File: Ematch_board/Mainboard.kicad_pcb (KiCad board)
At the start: 2 copper layers, 57.3 x 53.3 mm, 137 parts, among them J1 Conn_01x02_Male, J10 Conn_01x02_Male, J2 Conn_01x02_Male, J3 Conn_01x02_Male, J4 Conn_01x02_Male, J5 Conn_01x02_Male, J6 Conn_01x02_Male, J7 Conn_01x05_Male, J8 USB_C_Receptacle_USB2.0, J9 Conn_01x02_Male, Q1 MMDT2222A, Q2 MMDT2222A, Q51 PMV20ENR, Q52 PMV20ENR, Q53 PMV20ENR, Q54 PMV20ENR, Q55 PMV20ENR, Q56 PMV20ENR, U1 LTV-247, U2 LTC4411, U3 RT9025-25GSP, U4 LTC4411, U5 SN65HVD230, U6 CP2102-GMR-QFN28

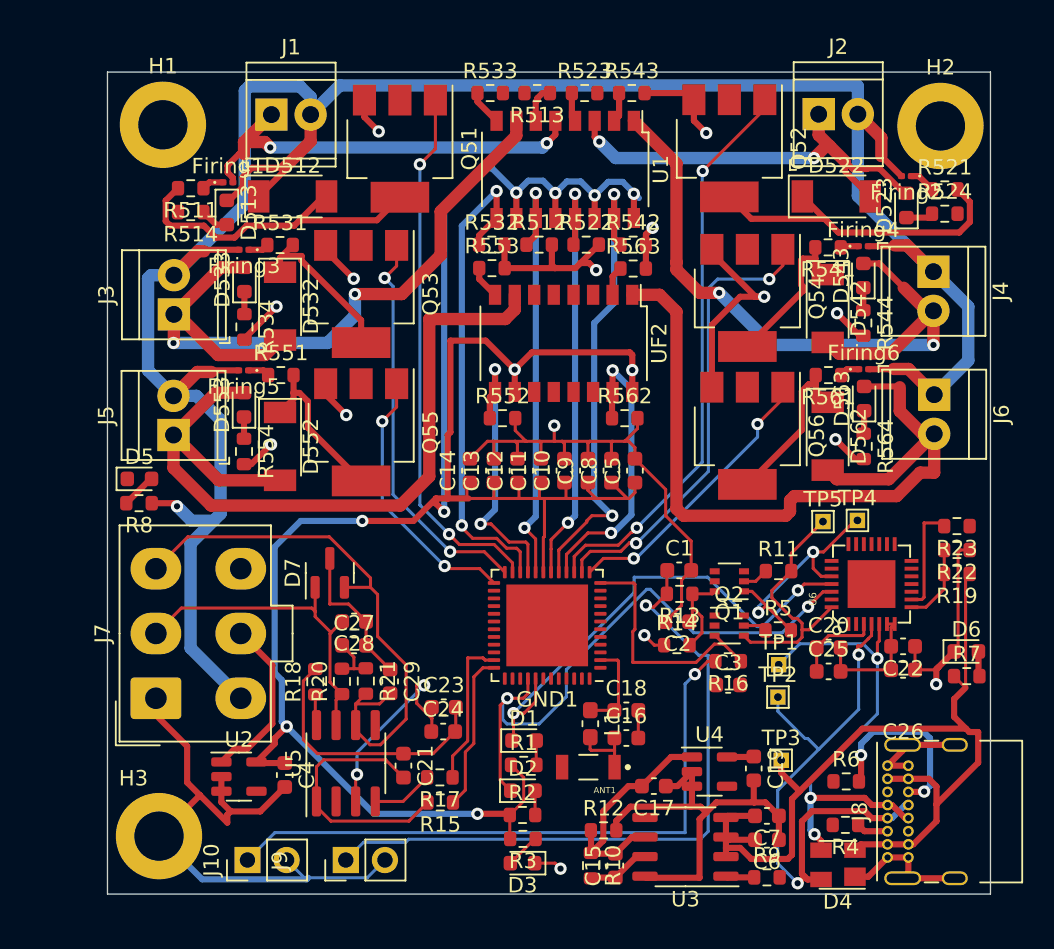
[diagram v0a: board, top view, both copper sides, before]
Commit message: removed ground traces
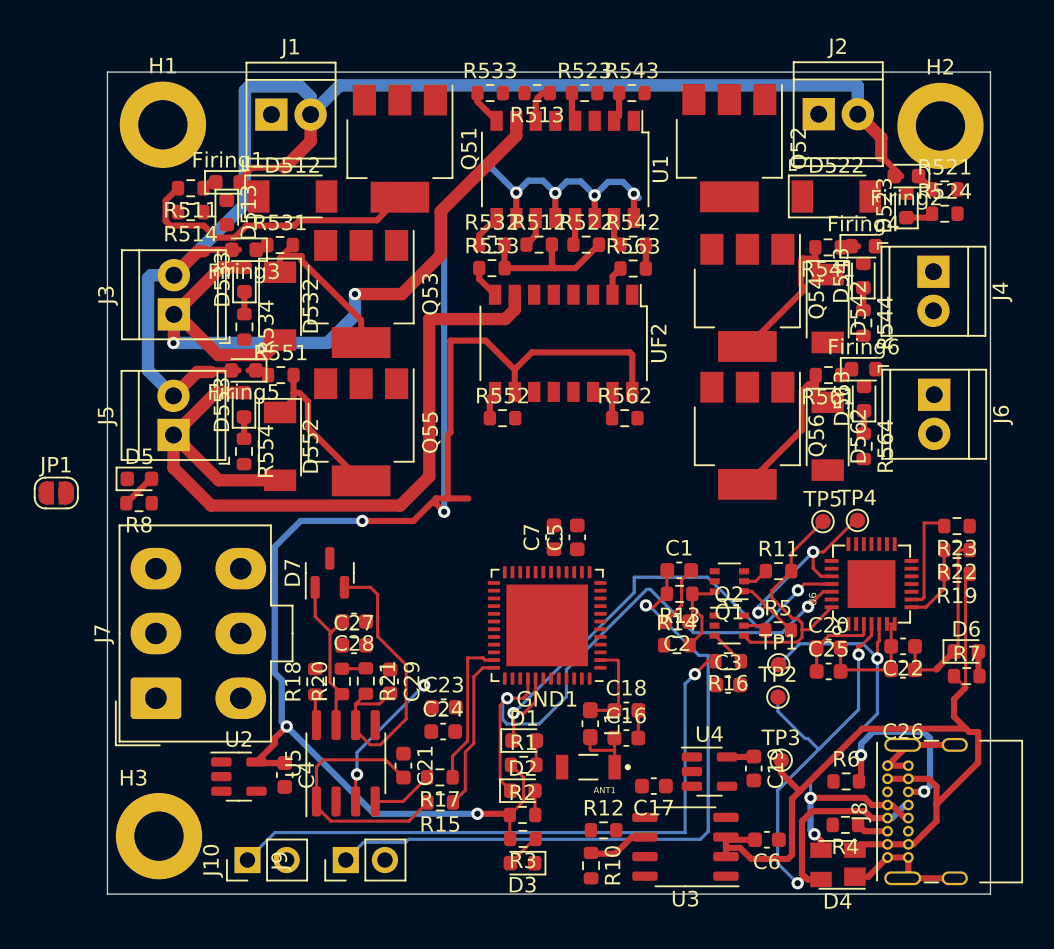
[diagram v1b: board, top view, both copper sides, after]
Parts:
- removed C10: 10uF, Capacitor_SMD:C_0603_1608Metric
- removed C11, C8: 1uF, Capacitor_SMD:C_0603_1608Metric
- removed C12, C13, C14, C15: 0.1uF, Capacitor_SMD:C_0603_1608Metric
- removed C9: 100pF, Capacitor_SMD:C_0603_1608Metric
- removed R9: 100k, Resistor_SMD:R_0603_1608Metric
- added JP1: SolderJumper_2_Open, Jumper:SolderJumper-2_P1.3mm_Open_RoundedPad1.0x1.5mm, F.Cu at (114.7, 96.8)
- C16: value 1.5pF -> 33pF
- C18: value 1.2pF -> 100pF
- C2: value 1nF -> 0.1uF
- C5: value 0.1uF -> 10uF
- C7: value 1uF -> 0.1uF
- Firing1, Firing2, Firing3, Firing4, Firing5, Firing6: footprint Diode_SMD:D_0201_0603Metric -> LED_SMD:LED_0603_1608Metric
- J7: value Conn_01x05_Male -> Conn_01x06_Female
- R10: value 147k -> 56k
- R12: value 47k -> 10K
- R15, R17: value 90 -> 120
- TP1, TP2, TP3, TP4, TP5: footprint TestPoint:TestPoint_THTPad_1.0x1.0mm_Drill0.5mm -> TestPoint:TestPoint_Pad_D1.0mm
- moved C7 22.7 mm to (146.9, 99.7), turned to 90 degrees
- moved C5 5.72 mm to (148.4, 99.7)
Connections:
- net Net-(C27-Pad1) renamed /Vref
- ANT1 pad 2: GND -> (no net)
- C7 pad 1: GND -> +3V3
- C7 pad 2: VBUS -> GND
- GND1 pad 12: /BOOT -> /Nuke 1
- GND1 pad 23: /Nuke 1 -> /BOOT
- GND1 pad 9: unconnected-(GND1-Pad9) -> /EN
- J7 pad 2: /CAN_HIGH -> GND
- J7 pad 3: /CAN_LOW -> Net-(J7-Pad3)
- J7 pad 5: Net-(U2-Pad1) -> /CAN_HIGH
- J7 pad 6: (no net) -> /CAN_LOW
- R8 pad 1: /24V -> +24V
- U2 pad 1: Net-(U2-Pad1) -> Net-(J7-Pad3)
- U3 pad 1: Net-(R9-Pad1) -> unconnected-(U3-Pad1)
- U3 pad 4: VBUS -> unconnected-(U3-Pad4)
- U5 pad 5: unconnected-(U5-Pad5) -> Net-(U5-Pad5)
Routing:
- net GND: track 219.0 -> 50.3 mm, vias 14 -> 0
- net /24V: track 154.9 -> 90.6 mm, vias 1 -> 0
- net Net-(D562-Pad2): track 52.2 -> 0.00 mm
- net Net-(D542-Pad2): track 45.8 -> 0.00 mm, vias 2 -> 0
- net /Nuke 2: track 37.0 -> 0.00 mm, vias 2 -> 0
- net /Nuke 1: track 34.8 -> 0.00 mm, vias 2 -> 0
- net +3V3: track 164.1 -> 133.0 mm, vias 13 -> 10
- net /ematch/Cont3: track 32.5 -> 2.20 mm, vias 2 -> 0
- net /Nuke 4: track 29.8 -> 0.00 mm, vias 2 -> 0
- net Net-(D512-Pad2): track 29.4 -> 0.00 mm, vias 2 -> 0
- net /ematch/Cont4: track 31.2 -> 1.90 mm, vias 2 -> 0
- net Net-(D522-Pad2): track 28.8 -> 0.00 mm, vias 2 -> 0
- net /ematch/Cont2: track 28.5 -> 1.62 mm, vias 2 -> 0
- net /ematch/Cont1: track 28.8 -> 1.98 mm, vias 2 -> 0
- net /Nuke 3: track 26.0 -> 0.00 mm, vias 2 -> 0
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
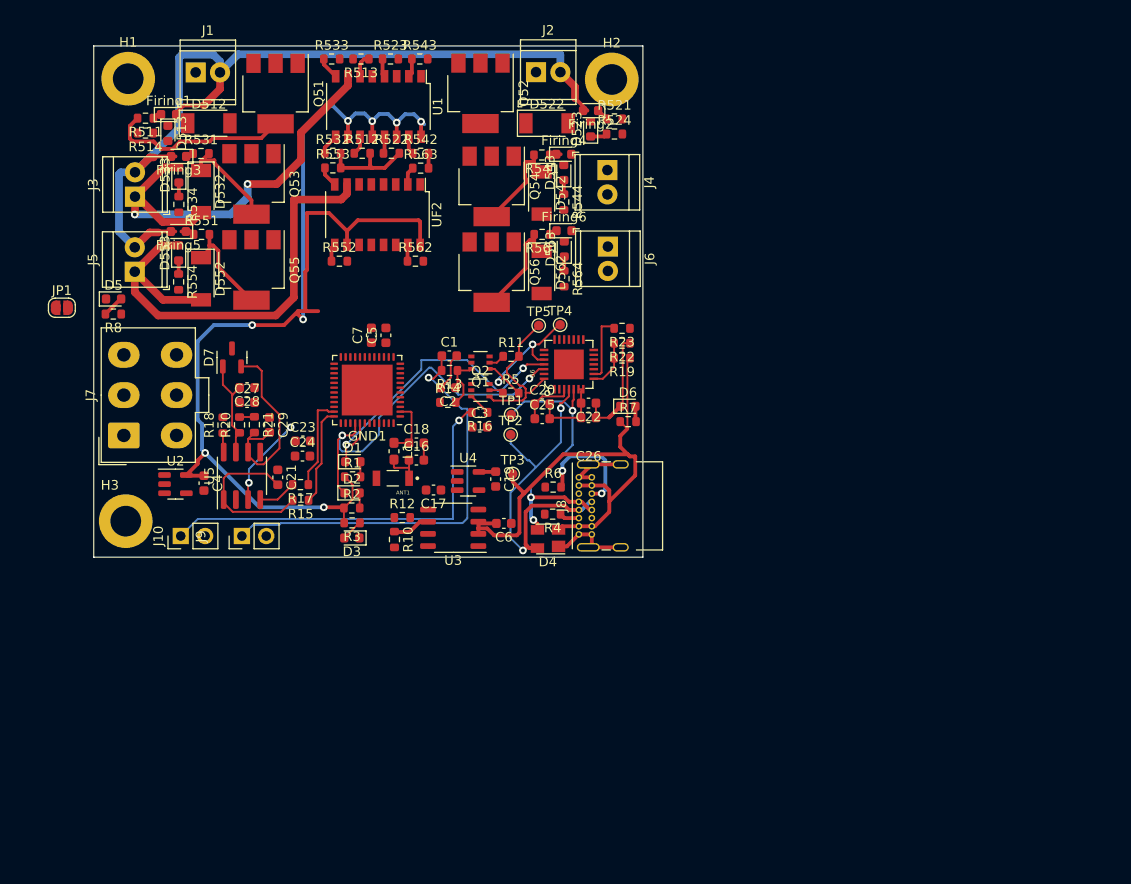
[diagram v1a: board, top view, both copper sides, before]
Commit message: routed thicker 24V traces and moved some components
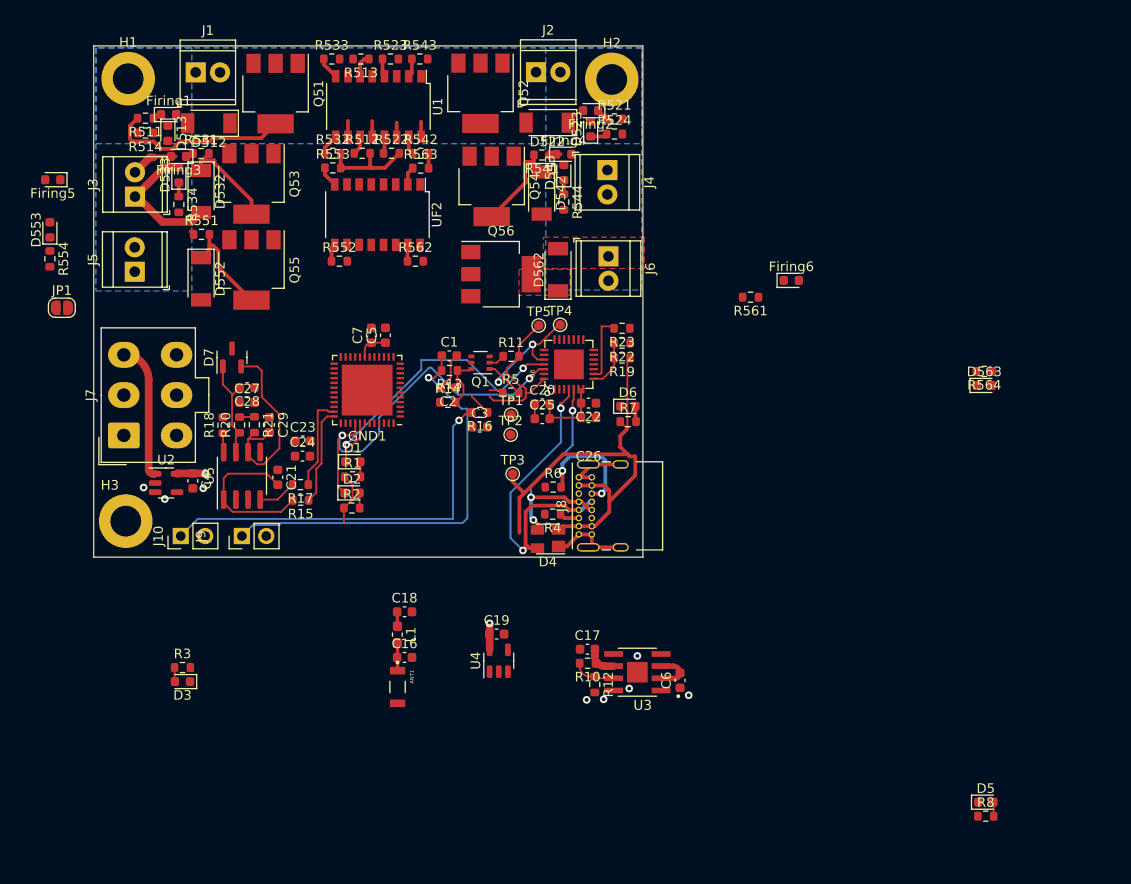
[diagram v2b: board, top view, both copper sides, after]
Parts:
- removed Q2: MMDT2222A, Package_TO_SOT_SMD:SOT-363_SC-70-6
- U3: footprint Package_SO:SOP-8_3.9x4.9mm_P1.27mm -> iclr:SOIC127P599X175-9N
- moved D5 105.0 mm to (211.0, 148.3)
- moved R8 104.9 mm to (211.0, 149.8), turned to 0 degrees
- moved D563 46.0 mm to (210.8, 104.9), turned to 0 degrees
- moved R564 44.9 mm to (210.8, 103.4), turned to 180 degrees
- moved R12 26.6 mm to (170.2, 136.1), turned to -90 degrees
- moved C6 24.6 mm to (179.1, 135.7), turned to 90 degrees
- moved U3 24.4 mm to (174.7, 134.8)
- moved Firing6 24.3 mm to (190.7, 94.0)
- moved R10 23.9 mm to (169.5, 133.9), turned to 180 degrees
- moved R3 23.2 mm to (127.2, 134.3), turned to 0 degrees
- moved D3 23.2 mm to (127.2, 135.8)
- moved C17 23.1 mm to (169.4, 132.4), turned to 0 degrees
- moved R561 22.7 mm to (186.4, 95.7)
- moved ANT1 21.8 mm to (149.7, 136.3), turned to -90 degrees
- moved C16 20.6 mm to (150.4, 133.3)
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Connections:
- C19 pad 1: /3.3V -> +3V3
- C20 pad 2: /3.3V -> +3V3
- C22 pad 2: /3.3V -> +3V3
- C25 pad 2: /3.3V -> +3V3
- C26 pad 2: /3.3V -> +3V3
- Q1 pad 3: (no net) -> /BOOT
- Q1 pad 4: (no net) -> /DTR
- Q52 pad 2: Net-(D522-Pad1) -> Net-(Q52-Pad2)
- Q52 pad 4: Net-(D522-Pad1) -> Net-(Q52-Pad2)
- R521 pad 2: Net-(D522-Pad1) -> Net-(Q52-Pad2)
- U4 pad 5: /3.3V -> +3V3
- U6 pad 6: /3.3V -> +3V3
- U6 pad 7: /3.3V -> +3V3
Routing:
- net +3V3: track 133.0 -> 29.2 mm, vias 10 -> 2
- net /24V: track 90.6 -> 5.56 mm
- net Net-(D552-Pad2): track 51.3 -> 0.00 mm
- net Net-(D532-Pad2): track 47.1 -> 14.0 mm, vias 2 -> 0
- net GND: track 50.3 -> 32.3 mm, vias 0 -> 8
- net Net-(J7-Pad3): track 0.00 -> 14.2 mm
- net Net-(D562-Pad1): track 10.7 -> 0.00 mm
- net /3.3V: track 10.00 -> 0.00 mm
- net /Data-: track 31.1 -> 23.7 mm
- net /Data+: track 37.8 -> 33.2 mm
- net Net-(R10-Pad2): track 0.00 -> 4.53 mm
- net /LNA_IN: track 5.68 -> 1.52 mm
- net VBUS: track 57.1 -> 53.8 mm
- net Net-(D563-Pad1): track 1.46 -> 0.00 mm
- net Net-(D553-Pad1): track 1.41 -> 0.00 mm
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- added copper zone on In2.Cu, net +3V3
- added copper zone on B.Cu, net /24V
- added copper zone on In1.Cu, net GND
- added copper zone on F.Cu, net Net-(D562-Pad1)
- added copper zone on F.Cu, net Net-(D562-Pad2)
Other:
- copper layers 2 -> 4

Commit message: changed schottky diode FP and rearranged mosfets + screw terminals
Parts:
- D512, D522, D532, D542, D552, D562: footprint Diode_SMD:D_SOD-128 -> Package_TO_SOT_SMD:TO-277B
- moved Firing4 51.4 mm to (216.9, 93.2)
- moved R541 50.8 mm to (213.9, 93.2)
- moved J6 46.3 mm to (216.6, 102.6)
- moved D562 45.9 mm to (210.6, 105.3), turned to 0 degrees
- moved D542 45.9 mm to (210.2, 90.7), turned to 0 degrees
- moved Q56 45.2 mm to (203.9, 105.7)
- moved J4 45.0 mm to (216.2, 88.0)
- moved Q54 44.6 mm to (203.6, 91.0), turned to 0 degrees
- moved D543 39.7 mm to (206.5, 86.7), turned to 0 degrees
- moved R544 36.6 mm to (203.5, 86.7), turned to 180 degrees
- moved R561 30.4 mm to (214.3, 107.9)
- moved Firing6 30.0 mm to (217.3, 107.9)
- moved C19 14.0 mm to (162.9, 144.5)
- moved U4 14.0 mm to (163.1, 147.3)
- moved C17 12.4 mm to (170.3, 144.8)
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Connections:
- D512 pad 2: Net-(D512-Pad2) -> Net-(D512-Pad1)
- D513 pad 2: Net-(D512-Pad2) -> Net-(D512-Pad1)
- D522 pad 1: Net-(Q52-Pad2) -> Net-(D523-Pad2)
- D522 pad 2: Net-(D522-Pad2) -> Net-(D523-Pad2)
- D523 pad 2: Net-(D522-Pad2) -> Net-(D523-Pad2)
- D532 pad 1: Net-(D532-Pad1) -> Net-(D533-Pad2)
- D532 pad 2: Net-(D532-Pad2) -> Net-(D533-Pad2)
- D533 pad 2: Net-(D532-Pad2) -> Net-(D533-Pad2)
- D542 pad 1: Net-(D542-Pad1) -> Net-(D543-Pad2)
- D542 pad 2: Net-(D542-Pad2) -> Net-(D543-Pad2)
- D543 pad 2: Net-(D542-Pad2) -> Net-(D543-Pad2)
- D552 pad 2: Net-(D552-Pad2) -> Net-(D552-Pad1)
- D553 pad 2: Net-(D552-Pad2) -> Net-(D552-Pad1)
- D562 pad 1: Net-(D562-Pad1) -> Net-(D563-Pad2)
- D562 pad 2: Net-(D562-Pad2) -> Net-(D563-Pad2)
- D563 pad 2: Net-(D562-Pad2) -> Net-(D563-Pad2)
- J1 pad 1: Net-(D512-Pad2) -> Net-(D512-Pad1)
- J2 pad 1: Net-(D522-Pad2) -> Net-(D523-Pad2)
- J3 pad 1: Net-(D532-Pad2) -> Net-(D533-Pad2)
- J4 pad 1: Net-(D542-Pad2) -> Net-(D543-Pad2)
- J5 pad 1: Net-(D552-Pad2) -> Net-(D552-Pad1)
- J6 pad 1: Net-(D562-Pad2) -> Net-(D563-Pad2)
- Q1 pad 5: (no net) -> Net-(Q1-Pad5)
- Q51 pad 2: Net-(D512-Pad1) -> Net-(D512-Pad3)
- Q51 pad 4: Net-(D512-Pad1) -> Net-(D512-Pad3)
- Q52 pad 2: Net-(Q52-Pad2) -> Net-(D522-Pad3)
- Q52 pad 4: Net-(Q52-Pad2) -> Net-(D522-Pad3)
- Q53 pad 2: Net-(D532-Pad1) -> Net-(D532-Pad3)
- Q53 pad 4: Net-(D532-Pad1) -> Net-(D532-Pad3)
- Q54 pad 2: Net-(D542-Pad1) -> Net-(D542-Pad3)
- Q54 pad 4: Net-(D542-Pad1) -> Net-(D542-Pad3)
- Q55 pad 2: Net-(D552-Pad1) -> Net-(D552-Pad3)
- Q55 pad 4: Net-(D552-Pad1) -> Net-(D552-Pad3)
- Q56 pad 2: Net-(D562-Pad1) -> Net-(D562-Pad3)
- Q56 pad 4: Net-(D562-Pad1) -> Net-(D562-Pad3)
- R511 pad 2: Net-(D512-Pad1) -> Net-(D512-Pad3)
- R521 pad 2: Net-(Q52-Pad2) -> Net-(D522-Pad3)
- R531 pad 2: Net-(D532-Pad1) -> Net-(D532-Pad3)
- R541 pad 2: Net-(D542-Pad1) -> Net-(D542-Pad3)
- R551 pad 2: Net-(D552-Pad1) -> Net-(D552-Pad3)
- R561 pad 2: Net-(D562-Pad1) -> Net-(D562-Pad3)
- U1 pad 1: Net-(D542-Pad2) -> Net-(D543-Pad2)
- U1 pad 3: Net-(D522-Pad2) -> Net-(D523-Pad2)
- U1 pad 5: Net-(D512-Pad2) -> Net-(D512-Pad1)
- U1 pad 7: Net-(D532-Pad2) -> Net-(D533-Pad2)
- UF2 pad 1: Net-(D562-Pad2) -> Net-(D563-Pad2)
- UF2 pad 7: Net-(D552-Pad2) -> Net-(D552-Pad1)
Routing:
- net Net-(D512-Pad3): track 0.00 -> 19.2 mm
- net Net-(D512-Pad1): track 19.2 -> 0.00 mm
- net Net-(D533-Pad2): track 0.00 -> 14.0 mm
- net Net-(D532-Pad2): track 14.0 -> 0.00 mm
- net Net-(Firing3-Pad1): track 0.43 -> 11.0 mm
- net Net-(D532-Pad1): track 10.6 -> 0.00 mm
- net Net-(D552-Pad3): track 0.00 -> 10.5 mm
- net Net-(D552-Pad1): track 10.5 -> 0.00 mm
- net Net-(D542-Pad1): track 10.2 -> 0.00 mm
- net /24V: track 5.56 -> 12.6 mm
- net Net-(D542-Pad3): track 0.00 -> 3.60 mm
- net Net-(D562-Pad3): track 0.00 -> 3.59 mm
- net Net-(D543-Pad2): track 0.00 -> 2.42 mm
- net Net-(D563-Pad2): track 0.00 -> 2.42 mm
- net Net-(D563-Pad1): track 0.00 -> 1.35 mm
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- added copper zone on F.Cu, net Net-(D542-Pad3)
- added copper zone on F.Cu, net Net-(D543-Pad2)
- added copper zone on F.Cu, net Net-(D562-Pad3)
- added copper zone on F.Cu, net Net-(D563-Pad2)
- removed copper zone on F.Cu, net Net-(D562-Pad1)
- removed copper zone on F.Cu, net Net-(D562-Pad2)
